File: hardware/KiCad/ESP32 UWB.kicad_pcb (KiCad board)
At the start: 2 copper layers, 72.3 x 32.6 mm, 56 parts, among them J2 HEADER-12P-2.54, J3 10118194-0001LF, Q1 S8050, Q2 S8050, SW1 BUTTON, SW2 BUTTON, U1 AMS1117-3.3, U2 ESP32-C3-MINI-1-N4, U3 SILICON_LABS_CP2102N-A01-GQFN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, U4 DWM1000

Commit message: fox pcb
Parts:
- C1, C10, C11, C12, C2, C3, C4, C5, C6, C7, C8, C9: footprint ESP32 UWB:0603 -> Capacitor_SMD:C_0603_1608Metric_Pad1.08x0.95mm_HandSolder
- D1: footprint ESP32 UWB:SOD323 -> Diode_SMD:D_SOD-323_HandSoldering
- D2, D3, D4, D5, D6: footprint ESP32 UWB:CHIPLED_0805_NOOUTLINE -> LED_SMD:LED_0805_2012Metric_Pad1.15x1.40mm_HandSolder
- J1: value (none) -> HEADER-20P-2.54; footprint ESP32 UWB:20P-2.54 -> Connector_PinHeader_2.54mm:PinHeader_1x20_P2.54mm_Vertical
- J2: footprint ESP32 UWB:12P-2.54 -> Connector_PinHeader_2.54mm:PinHeader_1x12_P2.54mm_Vertical
- J3: footprint ESP32 UWB:AMPHENOL_10118194-0001LF -> Connector_USB:USB_Micro-B_Amphenol_10118194_Horizontal
- LED1: value (none) -> SK6812_3535; footprint ESP32 UWB:LED3535 -> LED_SMD:LED_SK6812MINI_PLCC4_3.5x3.5mm_P1.75mm
- LED2, LED3: footprint ESP32 UWB:CHIPLED_0603_NOOUTLINE -> LED_SMD:LED_0603_1608Metric_Pad1.05x0.95mm_HandSolder
- Q1, Q2: footprint ESP32 UWB:SOT23 -> Package_TO_SOT_SMD:SOT-23
- R1, R10, R11, R12, R13, R14, R15, R16, R17, R18, R19, R2, R20, R21, R22, R3, R4, R5, R6, R7, R8, R9: footprint ESP32 UWB:0603 -> Resistor_SMD:R_0603_1608Metric_Pad0.98x0.95mm_HandSolder
- SJ1: value (none) -> SJS; footprint ESP32 UWB:SJ_S -> Jumper:SolderJumper-2_P1.3mm_Open_TrianglePad1.0x1.5mm
- SW1, SW2: footprint ESP32 UWB:157SW -> Button_Switch_SMD:SW_Push_SPST_NO_Alps_SKRK
- U1: footprint ESP32 UWB:SOT223 -> Package_TO_SOT_SMD:SOT-223-3_TabPin2
- U2: footprint ESP32 UWB:XCVR_ESP32-C3-MINI-1-N4 -> Espressif:ESP32-C3-MINI-1_Hand-Soldering
- U3: footprint ESP32 UWB:SILICON_LABS_CP2102N-A01-GQFN28_3 -> Package_DFN_QFN:QFN-28-1EP_5x5mm_P0.5mm_EP3.35x3.35mm
- moved J1 25.4 mm to (178.6, 90.9), turned to 90 degrees
- moved J2 13.9 mm to (178.6, 118.9)
- moved U2 2.79 mm to (179.0, 108.5)
- moved SW1 1.93 mm to (114.6, 113.3)
- moved SW2 1.63 mm to (114.6, 97.3)
- moved J3 1.34 mm to (115.2, 105.3)
- moved D4 0.76 mm to (144.8, 93.7), turned to 180 degrees
- moved D3 0.76 mm to (144.8, 95.8), turned to 180 degrees
- moved R17 0.67 mm to (150.9, 107.1)
- moved D1 0.51 mm to (118.9, 114.8), turned to 90 degrees
- moved R5 0.45 mm to (125.5, 95.6)
- moved R6 0.45 mm to (125.5, 92.2)
- moved LED3 0.43 mm to (127.0, 100.1), turned to 90 degrees
- moved C3 0.42 mm to (117.1, 115.1)
- moved C5 0.31 mm to (127.0, 118.4)
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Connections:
- net D+ renamed /D+
- net D- renamed /D-
- net DTR renamed /DTR
- net IO0 renamed /IO0
- net IO1 renamed /IO1
- net IO10 renamed /IO10
- net IO18 renamed /IO18
- net IO19 renamed /IO19
- net IO2 renamed /IO2
- net IO3 renamed /IO3
- net IO4/MOSI renamed /IO4/MOSI
- net IO5/MISO renamed /IO5/MISO
- net IO6/SCLK renamed /IO6/SCLK
- net IO7 renamed /IO7
- net IO8/CS renamed /IO8/CS
- net LEDRX renamed /LEDRX
- net LEDRXOK renamed /LEDRXOK
- net LEDSFD renamed /LEDSFD
- net LEDTX renamed /LEDTX
- net RESET renamed /RESET
- net RTS renamed /RTS
- net RXD renamed /RXD
- net TXD renamed /TXD
- C3 pad 1: VDD5V -> /VDD5V
- J2 pad 1: VDD5V -> /VDD5V
- J2 pad 7: IO9 -> /IO9
- J3 pad 4: (no net) -> unconnected-(J3-Pad4)
- Q1 pad 3: IO9 -> /IO9
- R1 pad 2: IO9 -> /IO9
- R12 pad 2: N$2 -> Net-(R12-Pad2)
- R13 pad 2: N$4 -> Net-(R13-Pad2)
- R19 pad 2: N$1 -> Net-(D3-Pad2)
- R2 pad 2: N$5 -> Net-(D2-Pad1)
- R20 pad 2: N$16 -> Net-(R20-Pad2)
- R21 pad 2: N$17 -> Net-(R21-Pad2)
- R22 pad 2: N$18 -> Net-(R22-Pad2)
- R4 pad 1: IO9 -> /IO9
- SJ1 pad 1: IO9 -> /IO9
- SJ1 pad 2: IO9 -> /IO9
- U1 pad 1: VDD5V -> GND
- U1 pad 2: GND -> +3V3
- U1 pad 3: +3V3 -> /VDD5V
- U2 pad 10: (no net) -> unconnected-(U2-Pad10)
- U2 pad 15: (no net) -> unconnected-(U2-Pad15)
- U2 pad 17: (no net) -> unconnected-(U2-Pad17)
- U2 pad 23: IO9 -> /IO9
- U2 pad 24: (no net) -> unconnected-(U2-Pad24)
- U2 pad 25: (no net) -> unconnected-(U2-Pad25)
- U2 pad 28: (no net) -> unconnected-(U2-Pad28)
- U2 pad 29: (no net) -> unconnected-(U2-Pad29)
- U2 pad 32: (no net) -> unconnected-(U2-Pad32)
- U2 pad 33: (no net) -> unconnected-(U2-Pad33)
- U2 pad 34: (no net) -> unconnected-(U2-Pad34)
- U2 pad 35: (no net) -> unconnected-(U2-Pad35)
- U2 pad 4: (no net) -> unconnected-(U2-Pad4)
- U2 pad 7: (no net) -> unconnected-(U2-Pad7)
- U2 pad 9: (no net) -> unconnected-(U2-Pad9)
- U3 pad 1: (no net) -> unconnected-(U3-Pad1)
- U3 pad 10: (no net) -> unconnected-(U3-Pad10)
- U3 pad 11: (no net) -> unconnected-(U3-Pad11)
- U3 pad 12: (no net) -> unconnected-(U3-Pad12)
- U3 pad 13: (no net) -> unconnected-(U3-Pad13)
- U3 pad 14: (no net) -> unconnected-(U3-Pad14)
- U3 pad 15: (no net) -> unconnected-(U3-Pad15)
- U3 pad 16: (no net) -> unconnected-(U3-Pad16)
- U3 pad 17: (no net) -> unconnected-(U3-Pad17)
- U3 pad 18: N$6 -> Net-(LED3-Pad1)
- U3 pad 19: N$3 -> Net-(LED2-Pad1)
- U3 pad 20: (no net) -> unconnected-(U3-Pad20)
- U3 pad 21: (no net) -> unconnected-(U3-Pad21)
- U3 pad 22: (no net) -> unconnected-(U3-Pad22)
- U4 pad GPIO4: (no net) -> unconnected-(U4-PadGPIO4)
- U4 pad GPIO5: (no net) -> unconnected-(U4-PadGPIO5)
- U4 pad GPIO6: (no net) -> unconnected-(U4-PadGPIO6)
- U4 pad GPIO7: (no net) -> unconnected-(U4-PadGPIO7)
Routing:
- net IO9: track 98.6 -> 0.00 mm, vias 4 -> 0
- net /IO9: track 0.00 -> 98.2 mm, vias 0 -> 4
- net /VDD5V: track 0.00 -> 97.4 mm, vias 0 -> 2
- net VDD5V: track 95.1 -> 0.00 mm, vias 2 -> 0
- net +3V3: track 186.5 -> 195.2 mm
- net /RTS: track 14.1 -> 20.1 mm
- net Net-(R5-Pad1): track 5.94 -> 0.00 mm
- net Net-(LED3-Pad1): track 0.00 -> 5.77 mm
- net N$6: track 5.77 -> 0.00 mm
- net Net-(LED2-Pad1): track 0.00 -> 5.42 mm
- net N$3: track 5.42 -> 0.00 mm
- net Net-(R12-Pad2): track 0.00 -> 3.29 mm
- net N$2: track 3.29 -> 0.00 mm
- net /IO1: track 46.4 -> 48.9 mm
- net Net-(D3-Pad2): track 0.00 -> 2.11 mm
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
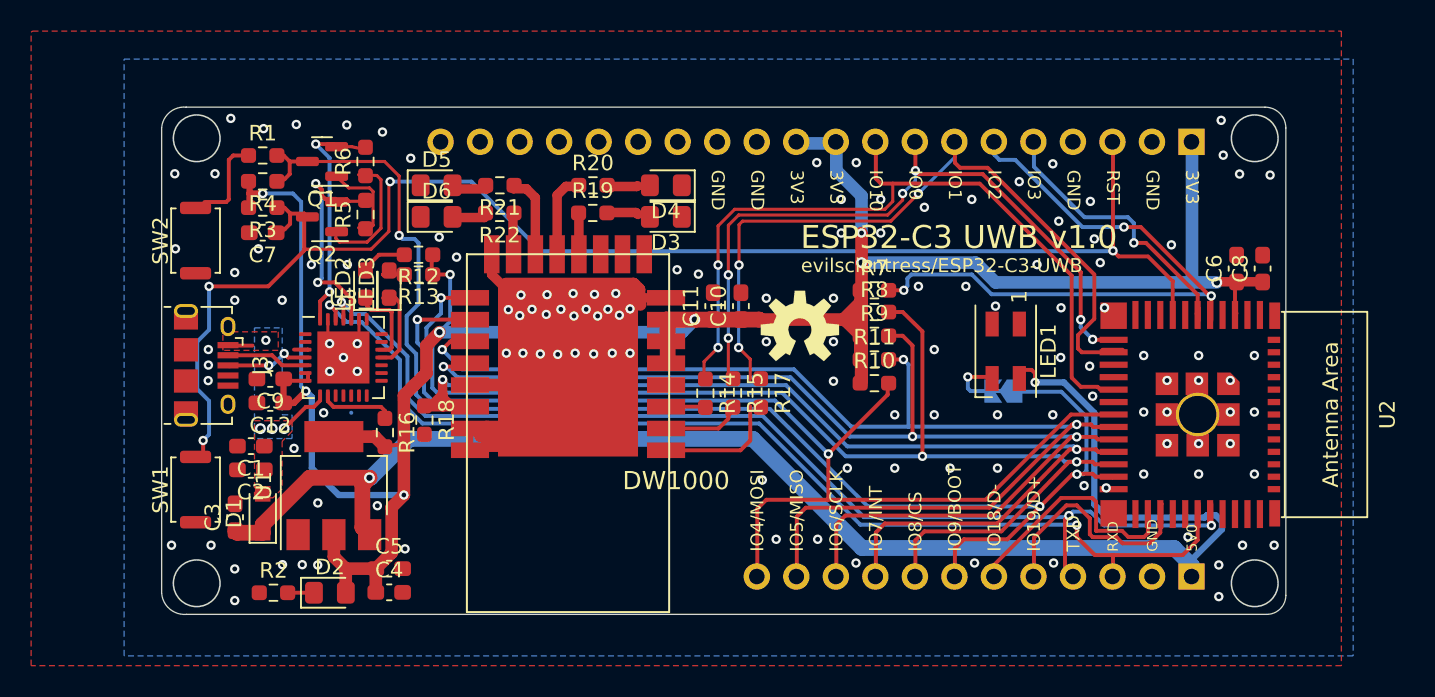
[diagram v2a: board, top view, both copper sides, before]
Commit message: tweak pcb and fix all DRC errors
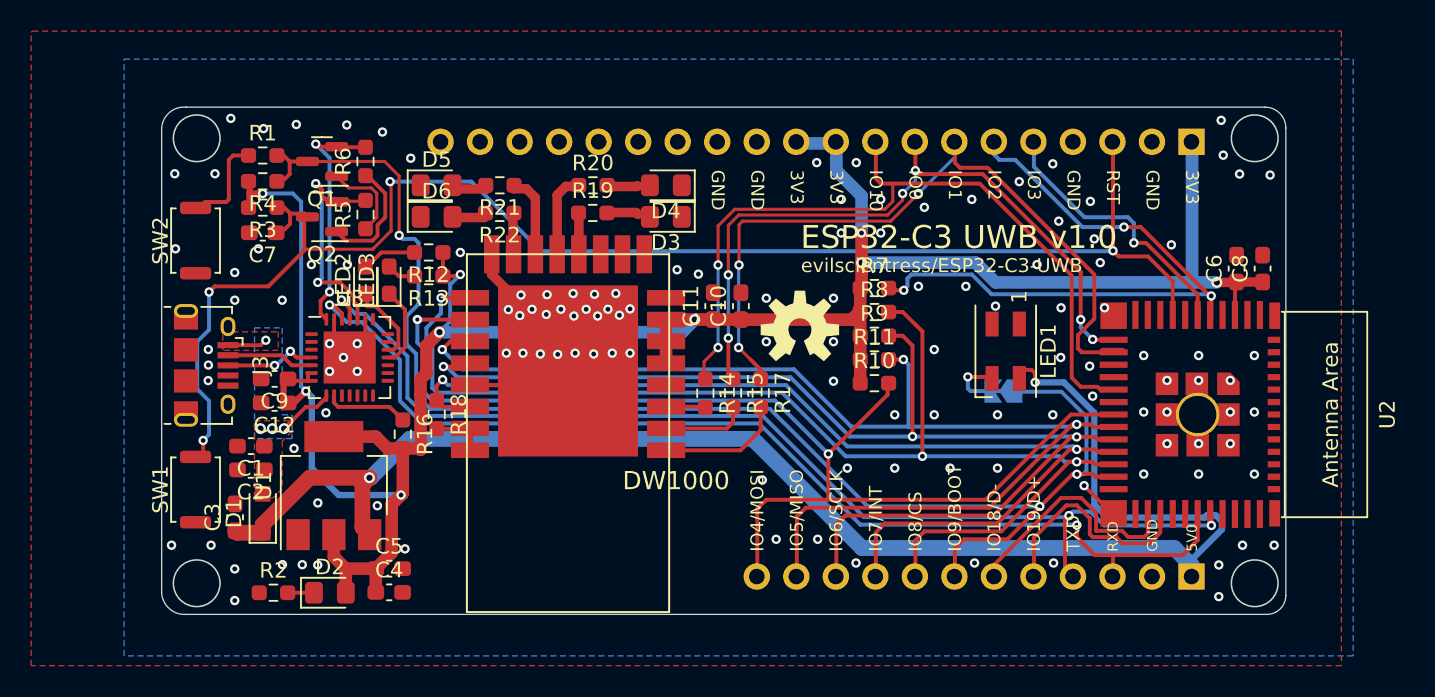
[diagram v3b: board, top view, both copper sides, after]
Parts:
- moved R16 1.15 mm to (127.9, 109.7)
- moved R18 0.86 mm to (130.0, 108.5)
- moved R12 0.67 mm to (129.5, 98.0)
- moved R13 0.66 mm to (129.5, 99.6)
- moved U3 0.40 mm to (124.5, 104.8)
- moved C12 0.27 mm to (119.6, 107.7)
- moved C9 0.27 mm to (119.6, 106.2)
- moved LED2 0.25 mm to (125.5, 99.8)
- moved LED3 0.25 mm to (127.0, 99.8)
- moved R7 0.15 mm to (158.2, 100.3)
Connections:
- U4 pad GND: (no net) -> GND
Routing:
- net +3V3: track 195.2 -> 159.9 mm
- net GND: track 44.3 -> 19.7 mm, vias 134 -> 131
- net /RTS: track 20.1 -> 14.3 mm
- net Net-(R5-Pad1): track 0.00 -> 5.63 mm
- net /IO7: track 69.6 -> 66.9 mm
- net /IO19: track 16.2 -> 14.7 mm
- net VBUS: track 5.17 -> 6.48 mm
- net Net-(R6-Pad1): track 8.69 -> 7.66 mm
- net Net-(LED3-Pad1): track 5.77 -> 5.24 mm
- net unconnected-(U2-Pad24): vias 1 -> 0

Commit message: first silkscreen tweaks
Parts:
- moved R14 0.66 mm to (147.3, 106.4)
- moved R15 0.65 mm to (149.1, 106.4)
- moved R17 0.65 mm to (150.9, 106.4)
- moved R19 0.28 mm to (140.2, 95.2)
- moved R20 0.28 mm to (140.2, 93.5)
- moved R22 0.25 mm to (134.1, 95.2)
- moved C7 0.25 mm to (118.9, 96.5)
- moved R21 0.25 mm to (134.1, 93.5)
- moved D5 0.25 mm to (130.3, 93.7)
- moved D6 0.25 mm to (130.3, 95.8)
- moved R3 0.17 mm to (118.9, 95.0)
- moved C6 0.15 mm to (181.6, 99.1)
- moved R1 0.14 mm to (118.9, 91.9)
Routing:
- net /RESET: track 96.0 -> 97.0 mm
- net Net-(D3-Pad2): track 2.11 -> 2.94 mm
- net Net-(R20-Pad2): track 2.05 -> 2.85 mm
- net /IO10: track 50.3 -> 49.5 mm
- net /IO0: track 45.1 -> 44.5 mm
- net /IO1: track 49.1 -> 48.5 mm
- net Net-(U4-PadEXTON): track 8.10 -> 7.50 mm

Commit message: more tweaks
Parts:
- U2: footprint Espressif:ESP32-C3-MINI-1_Hand-Soldering -> Espressif:ESP32-C3-MINI-1
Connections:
- U4 pad GND: GND -> (no net)

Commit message: tweak silkscreen and 3d model
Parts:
- removed the R1 at (118.9, 91.9)
- added R3: 470R, Resistor_SMD:R_0603_1608Metric_Pad0.98x0.95mm_HandSolder, F.Cu at (118.9, 91.9)
- U2: footprint Espressif:ESP32-C3-MINI-1 -> Espressif:ESP32-C3-MINI-1_Hand-Soldering
- moved SW1 1.52 mm to (114.6, 114.8)
- moved R21 0.57 mm to (134.6, 95.0)
- moved R19 0.51 mm to (134.6, 93.5)
- moved R22 0.25 mm to (140.2, 95.0)
- moved R5 0.15 mm to (125.5, 95.8)
- renumbered C12 to C10, C10 to C12, C5 to C4, C4 to C5, C8 to C7, C7 to C8, D6 to D3, D5 to D4, D3 to D5, D4 to D6, LED2 to D7, LED3 to D8, R3 to R1, R8 to R10, R9 to R11, R11 to R12, R10 to R13, R17 to R16, R16 to R17, R21 to R19, R4 to R2, R22 to R21, R19 to R22, R2 to R4, R12 to R7, R13 to R8, R7 to R9, LED1 to U5
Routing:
- net +3V3: track 159.9 -> 161.7 mm
- net /LEDRXOK: track 2.51 -> 3.39 mm
- net Net-(R21-Pad2): track 2.09 -> 2.82 mm
- net Net-(R19-Pad2): track 2.08 -> 2.71 mm
- net /RESET: track 97.0 -> 97.6 mm
- net /LEDTX: track 2.65 -> 3.21 mm
- net /DTR: vias 2 -> 3

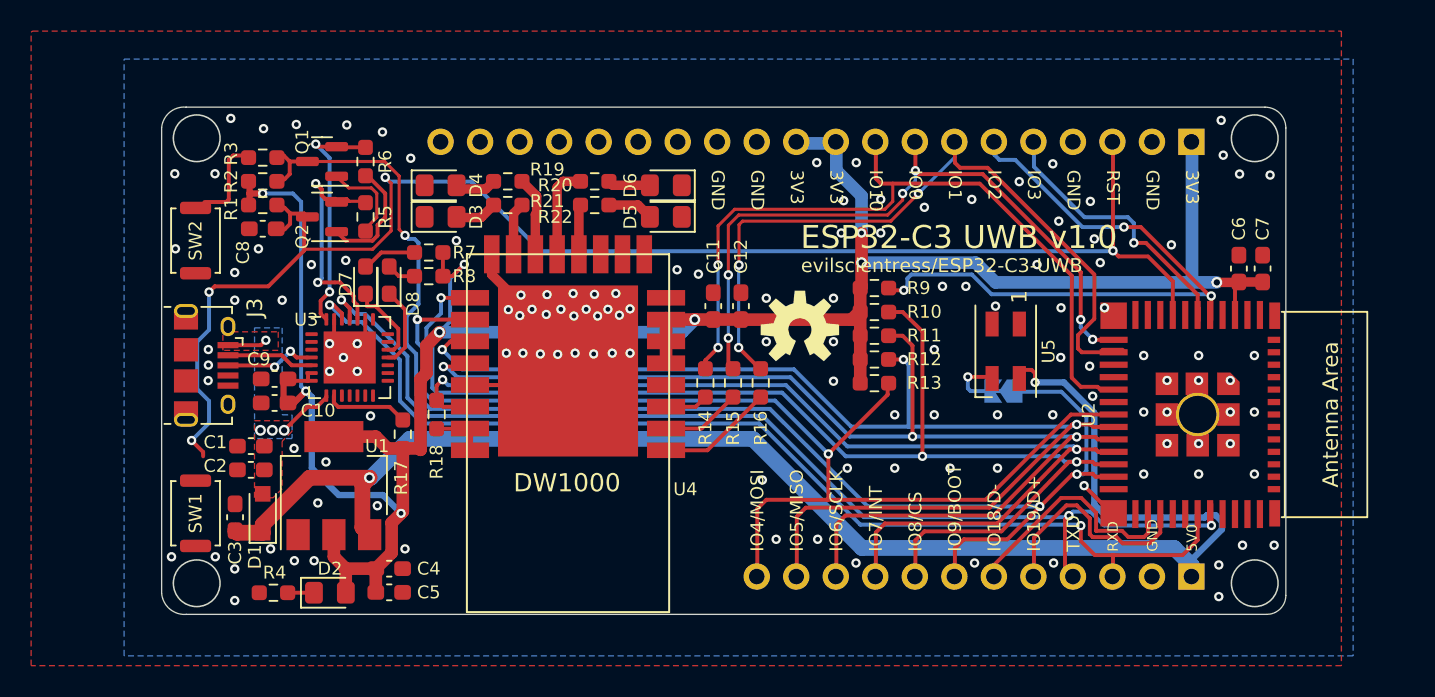
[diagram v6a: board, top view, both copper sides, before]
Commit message: tweak silkscreen orientation and more
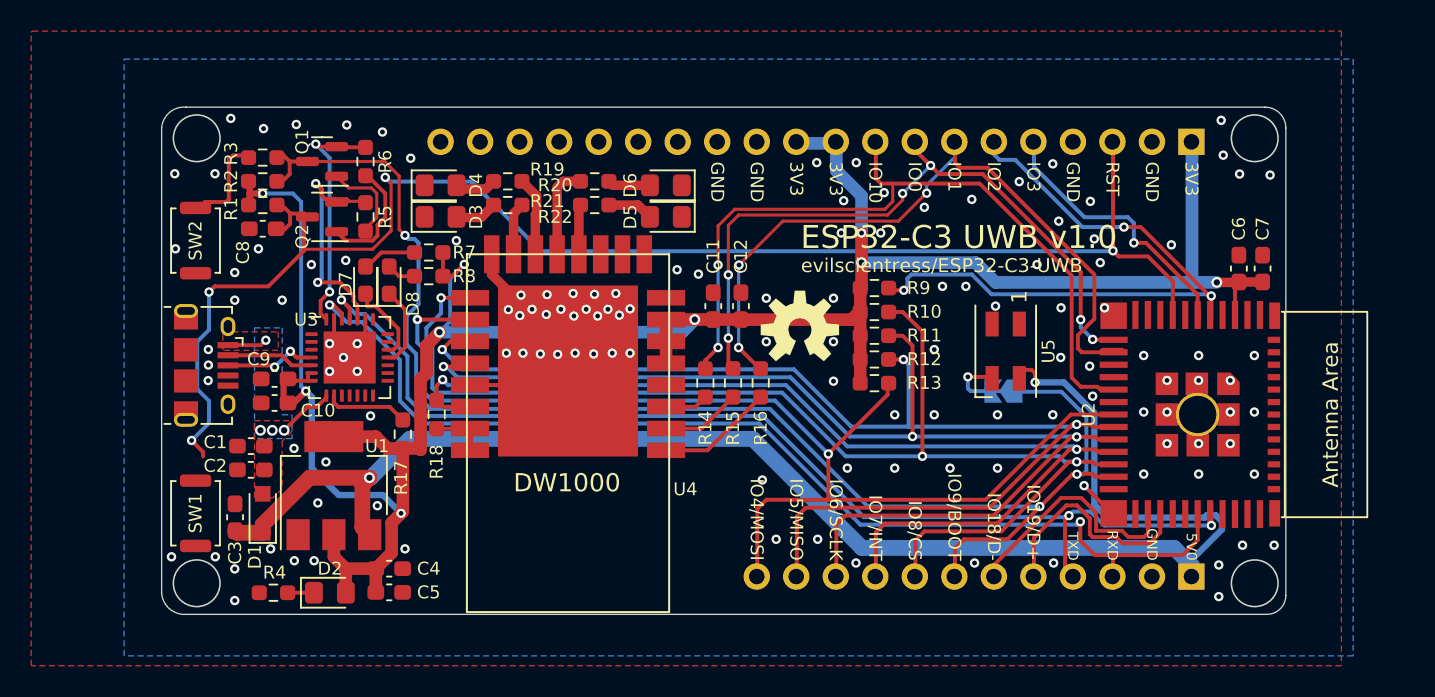
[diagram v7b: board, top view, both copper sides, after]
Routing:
- net /IO1: track 48.5 -> 47.3 mm

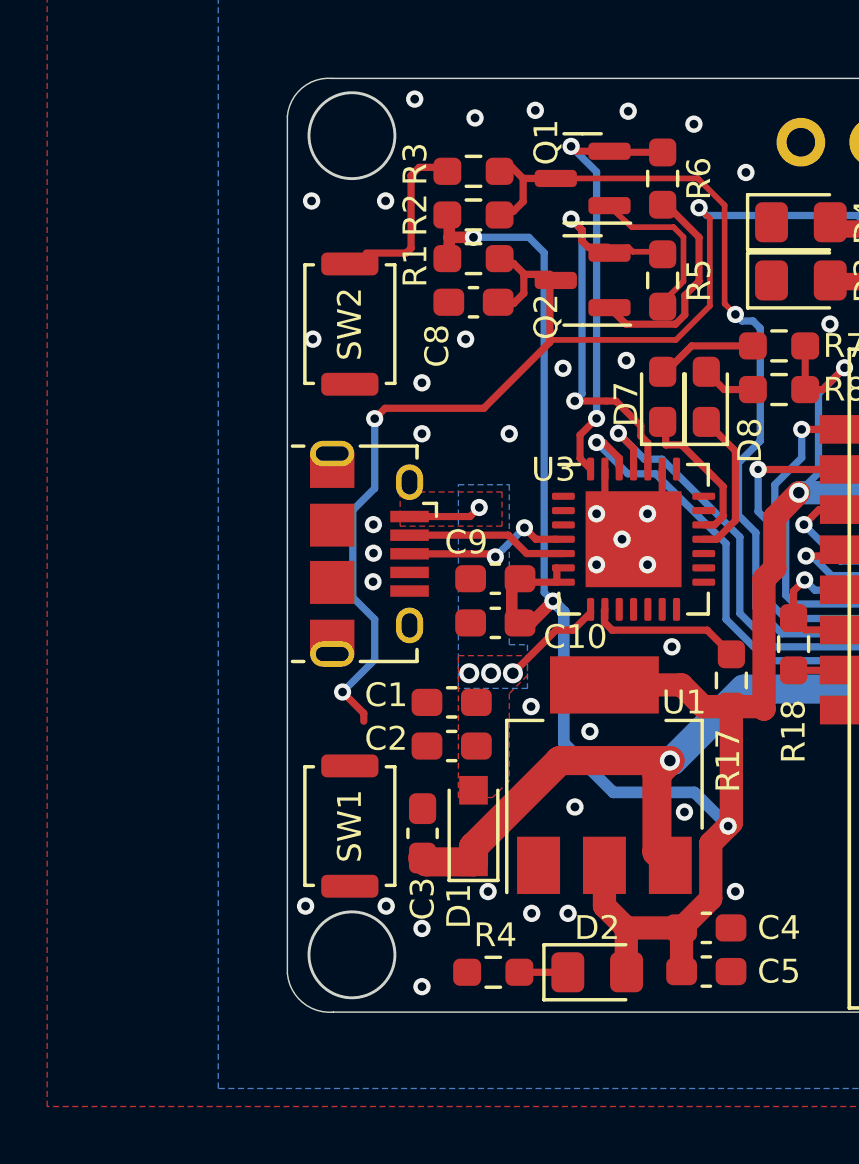
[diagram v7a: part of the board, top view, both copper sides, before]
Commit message: swap pushbuttons
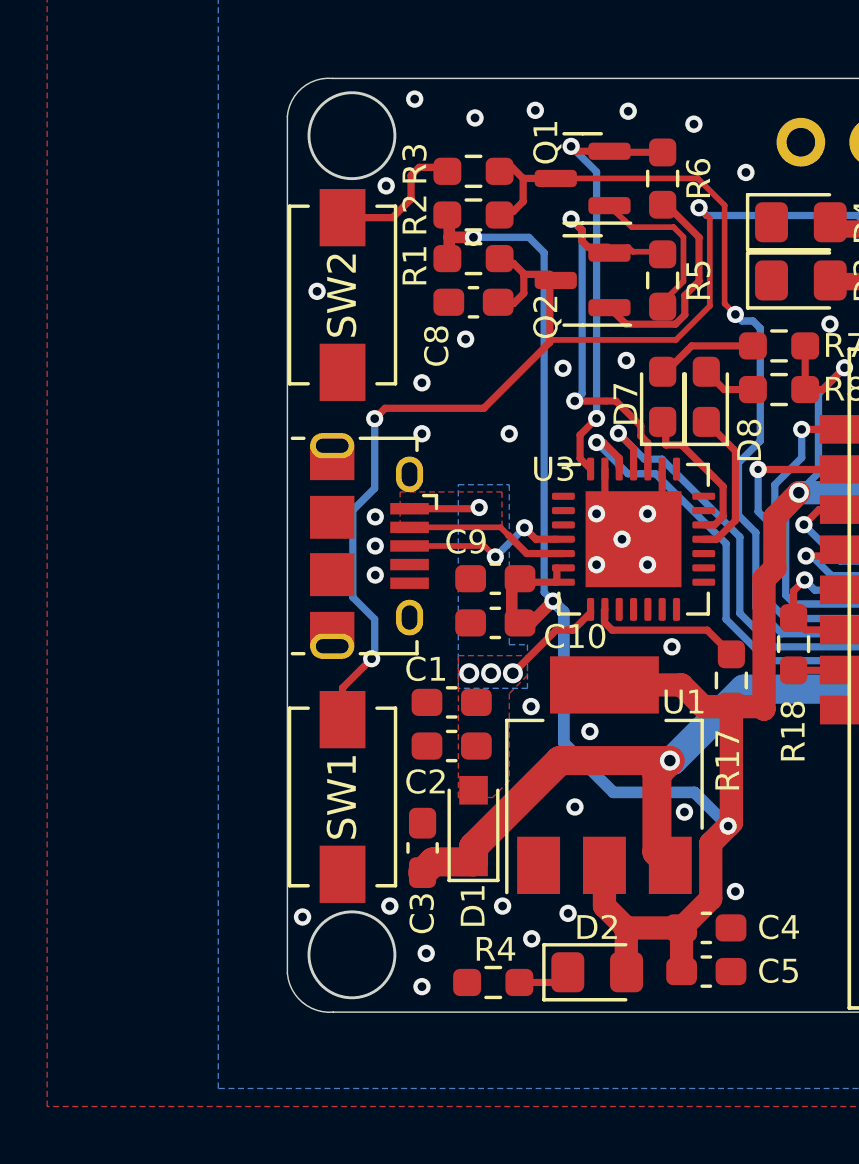
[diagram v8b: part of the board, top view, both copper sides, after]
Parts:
- SW1, SW2: footprint Button_Switch_SMD:SW_Push_SPST_NO_Alps_SKRK -> Button_Switch_SMD:SW_SPST_EVQPE1
- moved SW1 1.05 mm to (114.3, 113.8)
- moved SW2 1.05 mm to (114.3, 96.3)
- moved C3 0.51 mm to (117.1, 115.6)
- moved R4 0.36 mm to (119.6, 120.3)
- moved J3 0.27 mm to (115.2, 105.0)
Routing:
- net Net-(R3-Pad1): track 5.62 -> 4.93 mm
- net GND: vias 131 -> 130
